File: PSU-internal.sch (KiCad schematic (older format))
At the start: 56 parts, among them Q1 BD241A, Q2 BD241A, Q3 BD242, U1 OPA27, U2 OPA27, U3 OPA27, U4 2N6507, U5 2N6507, U6 2N6507, U7 REF02, U8 2N6507, U9 OPA27

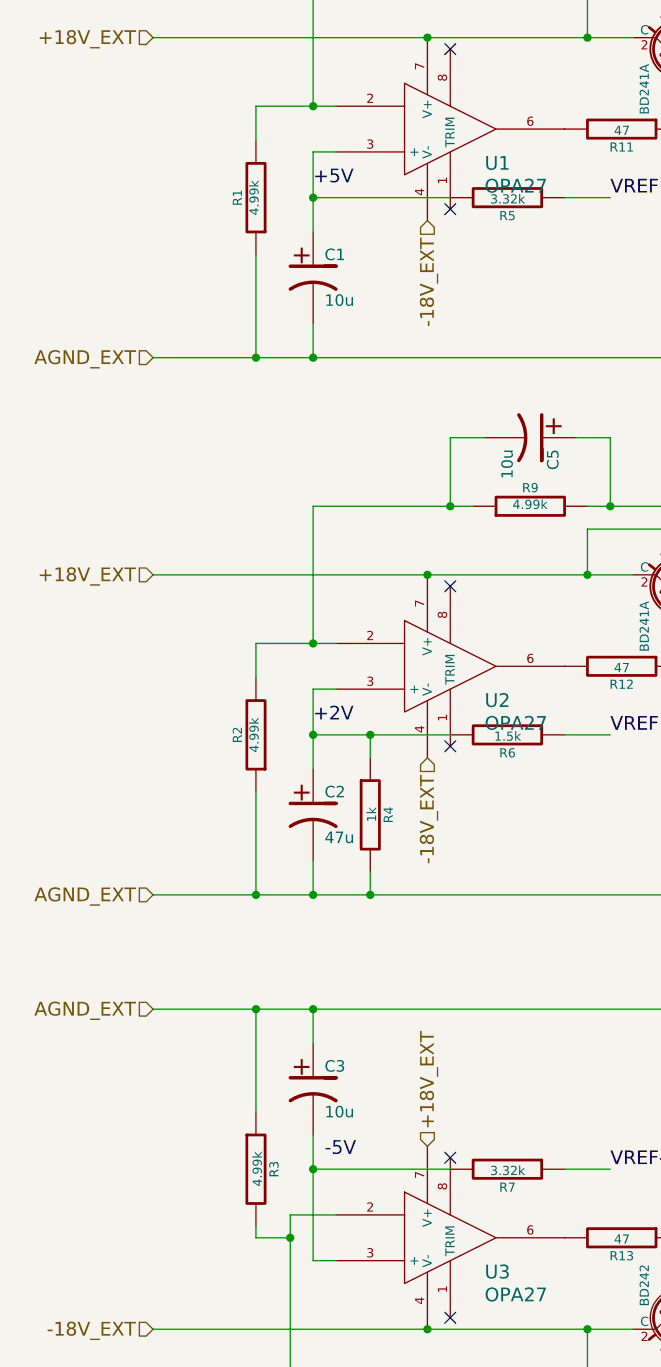
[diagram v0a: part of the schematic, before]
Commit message: Added vias for ground-connected pins that cannot be soldered from the top, as I can't make PTHs. Rearranged the power inputs slightly.
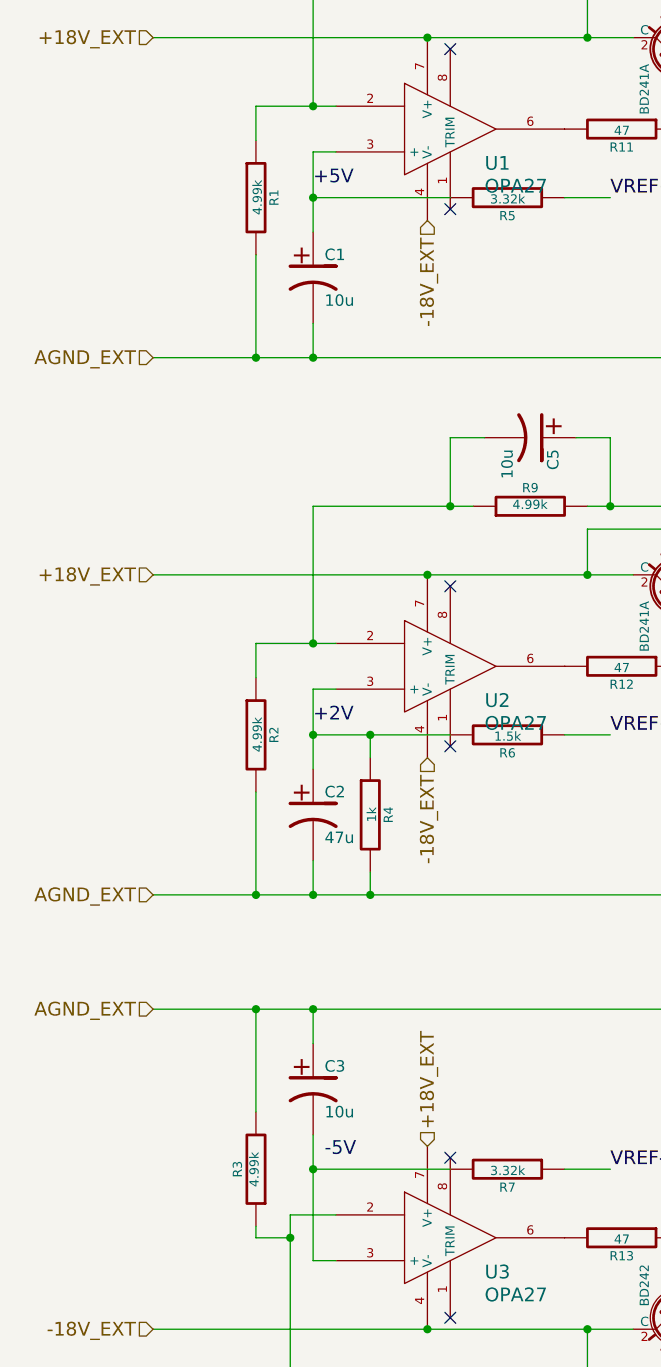
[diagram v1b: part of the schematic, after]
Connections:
- net AGND: now also R1.2, R2.2, R3.2; no longer R1.1, R2.1, R3.1
- net at C4.2, R8.1, U1.2: now also R1.1; no longer R1.2
- net at C5.2, R9.1, U2.2: now also R2.1; no longer R2.2
- net at C6.1, R10.1, U3.2: now also R3.1; no longer R3.2
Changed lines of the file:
@@
 F 4 "4.99KXBK-ND" V 1800 4350 60  0001 C CNN "DigiKey"
 	1    1800 4350
-	-1   0    0    1
+	1    0    0    -1
 $EndComp
 $Comp
@@
 F 4 "4.99KXBK-ND" V 1800 2000 60  0001 C CNN "DigiKey"
 	1    1800 2000
-	-1   0    0    1
+	1    0    0    -1
 $EndComp
 $Comp
@@
 F 4 "4.99KXBK-ND" V 1800 6250 60  0001 C CNN "DigiKey"
 	1    1800 6250
-	1    0    0    -1
+	-1   0    0    1
 $EndComp
 $Comp
